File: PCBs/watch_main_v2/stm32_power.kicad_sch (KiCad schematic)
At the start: 23 parts, among them U801 STM32U5A9NJH6Q

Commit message: Schematic v2 complete
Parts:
- added C922: 100n, Capacitor_SMD:C_0402_1005Metric, symbol Device:C_Small
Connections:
- net +1V8: no longer U801.E9 (VDDUSB)
- net +3V3: now also U801.E9 (VDDUSB), C922.1
- net GND: now also C922.2
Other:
- note added: "VDDUSB"
- moved on the sheet: C912, C914, C916

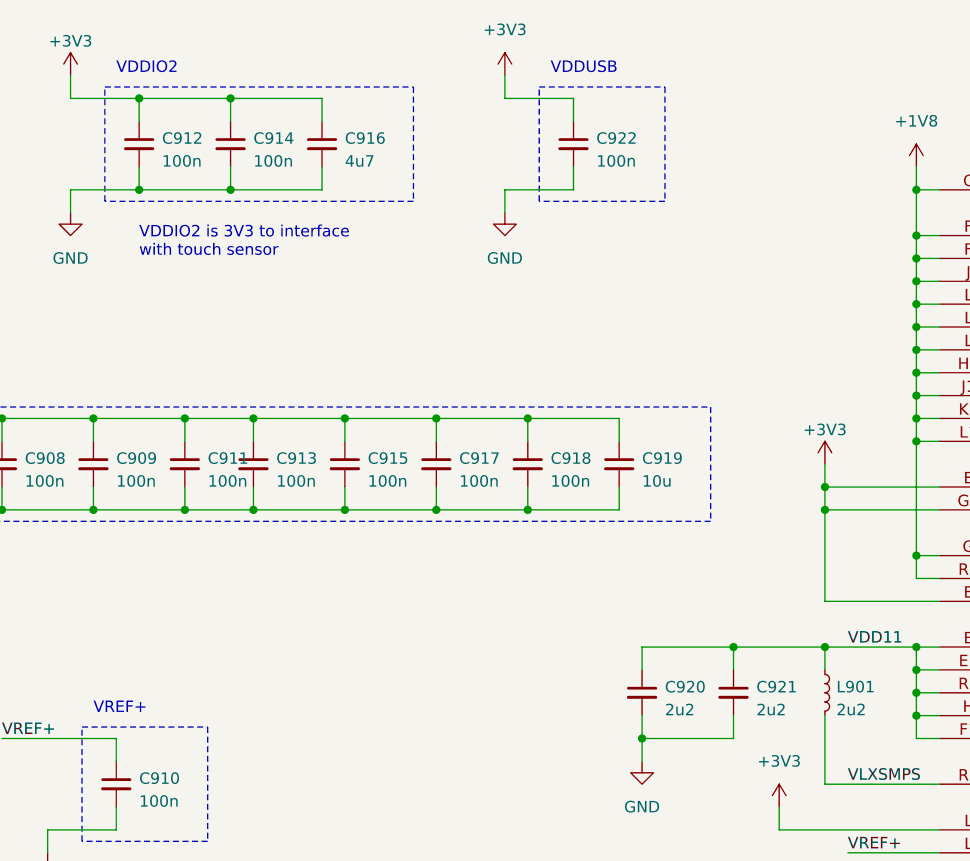
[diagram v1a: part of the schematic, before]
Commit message: 262 Unrouted traces, fixed clearance issues
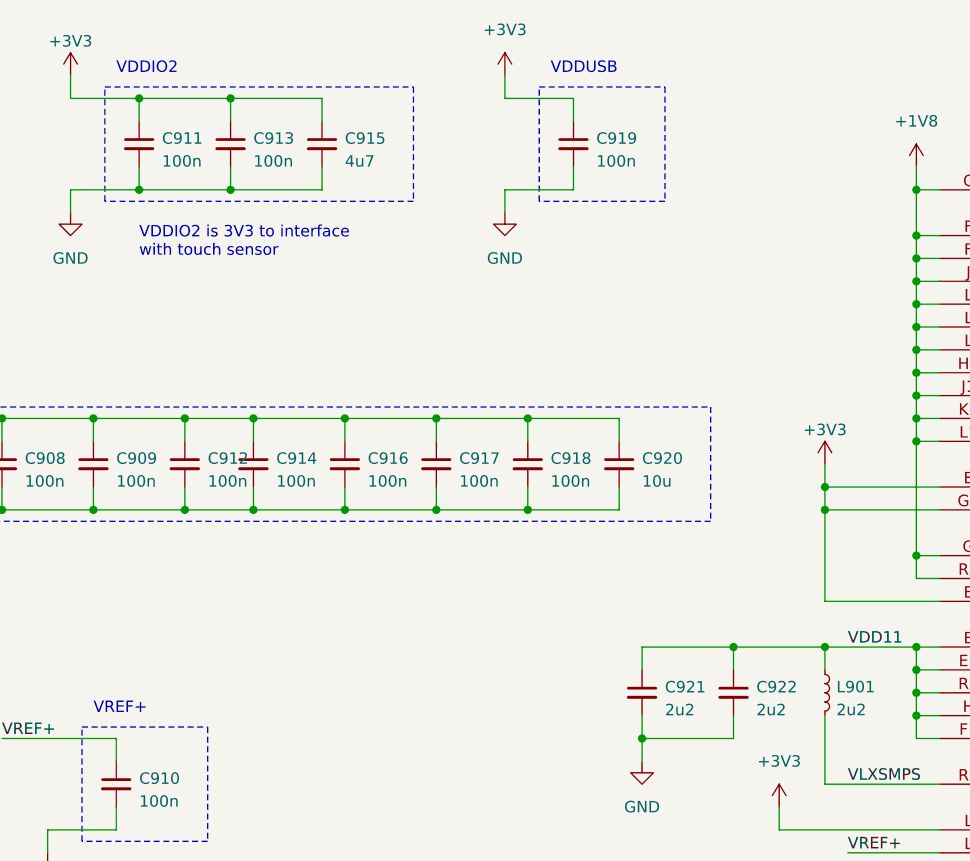
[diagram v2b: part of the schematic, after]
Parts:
- renumbered C912 to C911, C911 to C912, C914 to C913, C913 to C914, C916 to C915, C915 to C916, C922 to C919, C919 to C920, C920 to C921, C921 to C922
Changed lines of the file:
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@@
   (symbol (lib_id "Device:C_Small") (at 106.68 53.34 0) (unit 1)
     (in_bom yes) (on_board yes) (dnp no)
-    (property "Reference" "C916" (at 109.22 52.7113 0)
+    (property "Reference" "C915" (at 109.22 52.7113 0)
       (effects (font (size 1.27 1.27)) (justify left))
     )
@@
   (symbol (lib_id "Device:C_Small") (at 109.22 88.9 0) (unit 1)
     (in_bom yes) (on_board yes) (dnp no)
-    (property "Reference" "C915" (at 111.76 88.2713 0)
+    (property "Reference" "C916" (at 111.76 88.2713 0)
       (effects (font (size 1.27 1.27)) (justify left))
     )
@@
   (symbol (lib_id "Device:C_Small") (at 152.4 114.3 0) (unit 1)
     (in_bom yes) (on_board yes) (dnp no)
-    (property "Reference" "C921" (at 154.94 113.6713 0)
+    (property "Reference" "C922" (at 154.94 113.6713 0)
       (effects (font (size 1.27 1.27)) (justify left))
     )
@@
   (symbol (lib_id "Device:C_Small") (at 142.24 114.3 0) (unit 1)
     (in_bom yes) (on_board yes) (dnp no)
-    (property "Reference" "C920" (at 144.78 113.6713 0)
+    (property "Reference" "C921" (at 144.78 113.6713 0)
       (effects (font (size 1.27 1.27)) (justify left))
     )
@@
   (symbol (lib_id "Device:C_Small") (at 91.44 88.9 0) (unit 1)
     (in_bom yes) (on_board yes) (dnp no)
-    (property "Reference" "C911" (at 93.98 88.2713 0)
+    (property "Reference" "C912" (at 93.98 88.2713 0)
       (effects (font (size 1.27 1.27)) (justify left))
     )
@@
   (symbol (lib_id "Device:C_Small") (at 139.7 88.9 0) (unit 1)
     (in_bom yes) (on_board yes) (dnp no)
-    (property "Reference" "C919" (at 142.24 88.2713 0)
+    (property "Reference" "C920" (at 142.24 88.2713 0)
       (effects (font (size 1.27 1.27)) (justify left))
     )
@@
   (symbol (lib_id "power:+3V3") (at 162.56 88.9 0) (unit 1)
     (in_bom yes) (on_board yes) (dnp no) (fields_autoplaced)
-    (property "Reference" "#PWR0912" (at 162.56 92.71 0)
+    (property "Reference" "#PWR0914" (at 162.56 92.71 0)
       (effects (font (size 1.27 1.27)) hide)
     )
@@
   (symbol (lib_id "Device:C_Small") (at 86.36 53.34 0) (unit 1)
     (in_bom yes) (on_board yes) (dnp no)
-    (property "Reference" "C912" (at 88.9 52.7113 0)
+    (property "Reference" "C911" (at 88.9 52.7113 0)
       (effects (font (size 1.27 1.27)) (justify left))
     )
@@
   (symbol (lib_id "Device:C_Small") (at 134.62 53.34 0) (unit 1)
     (in_bom yes) (on_board yes) (dnp no)
-    (property "Reference" "C922" (at 137.16 52.7113 0)
+    (property "Reference" "C919" (at 137.16 52.7113 0)
       (effects (font (size 1.27 1.27)) (justify left))
     )
@@
   (symbol (lib_id "Device:C_Small") (at 96.52 53.34 0) (unit 1)
     (in_bom yes) (on_board yes) (dnp no)
-    (property "Reference" "C914" (at 99.06 52.7113 0)
+    (property "Reference" "C913" (at 99.06 52.7113 0)
       (effects (font (size 1.27 1.27)) (justify left))
     )
@@
   (symbol (lib_id "Device:C_Small") (at 99.06 88.9 0) (unit 1)
     (in_bom yes) (on_board yes) (dnp no)
-    (property "Reference" "C913" (at 101.6 88.2713 0)
-      (effects (font (size 1.27 1.27)) (justify left))
-    )
+    (property "Reference" "C914" (at 101.6 88.2713 0)
+      (effects (font (size 1.27 1.27)) (justify left))
+    )

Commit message: 190 Unrouted traces
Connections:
- net +1V8: now also C903.1, C905.1, C911.1, C913.1, C915.1, U801.E8 (VDDIO2), U801.G11 (VDDIO2), U801.L6 (VDDA)
- net +3V3: no longer C903.1, C905.1, C911.1, C913.1, C915.1, U801.E8 (VDDIO2), U801.G11 (VDDIO2), U801.L6 (VDDA)
